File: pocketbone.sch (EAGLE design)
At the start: 61 parts, among them J1 USD_CONNECTOR, U1 24LC_32AT-I/OT, U2 OSD3358, U3 SN74LVC1G07_DCK_5, Y1 CM200C-32.768KAZF-UT, Y2 445C33D24M00000

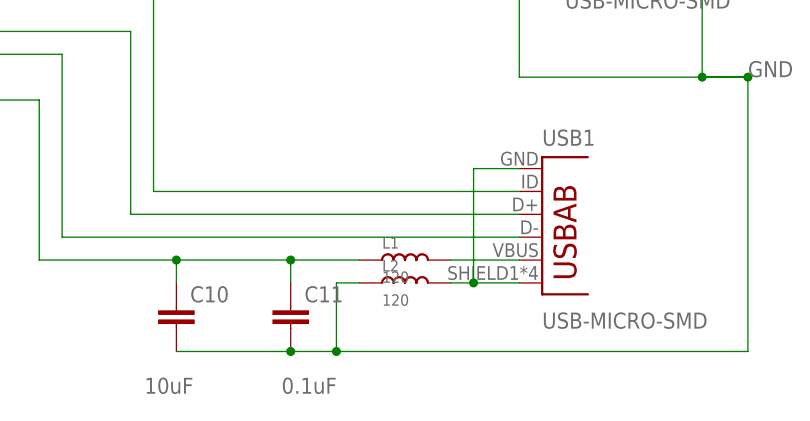
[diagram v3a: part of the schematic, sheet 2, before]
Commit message: Resize some silkscreen
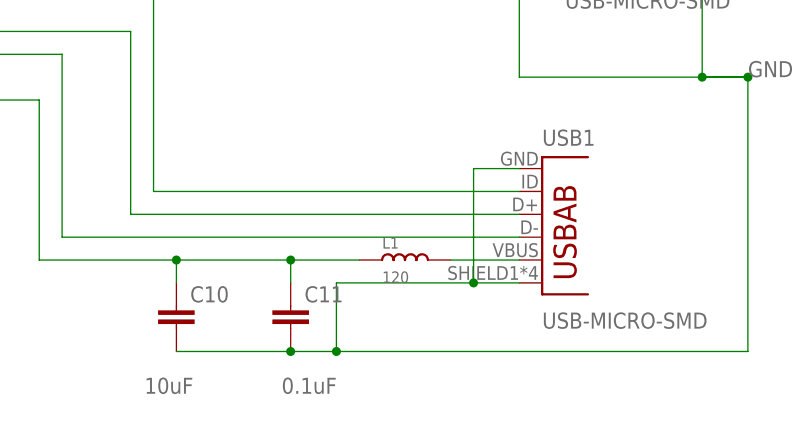
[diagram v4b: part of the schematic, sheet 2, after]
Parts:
- removed L2: 120, Seeed-OPL-Inductor:INDUCTOR/FERRITE-BEAD'0603'
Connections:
- removed net N$128: L2.2, USB1.GND, USB1.SHIELD
- net GND: now also USB1.GND, USB1.SHIELD; no longer L2.1
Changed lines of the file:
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@@
 <part name="R11" library="Strawson_Eagle_Lib" deviceset="RESISTOR" device="0402-RES" value="0"/>
 <part name="R12" library="Strawson_Eagle_Lib" deviceset="RESISTOR" device="0402-RES" value="0,DNI"/>
-<part name="L2" library="Seeed-OPL-Inductor" deviceset="INDUCTOR/FERRITE-BEAD" device="'0603'" value="120"/>
 <part name="L1" library="Seeed-OPL-Inductor" deviceset="INDUCTOR/FERRITE-BEAD" device="'0603'" value="120"/>
 <part name="C11" library="Strawson_Eagle_Lib" deviceset="CAP" device="0402-CAP" value="0.1uF"/>
@@
 <attribute name="VALUE" x="125.73" y="65.278" size="1.27" layer="96" align="center-left"/>
 </instance>
-<instance part="L2" gate="L" x="304.8" y="60.96"/>
 <instance part="L1" gate="L" x="304.8" y="63.5"/>
 <instance part="C11" gate="G$1" x="292.1" y="55.88" smashed="yes">
@@
 <wire x1="297.18" y1="53.34" x2="297.18" y2="60.96" width="0.1524" layer="91"/>
 <junction x="297.18" y="53.34"/>
-<pinref part="L2" gate="L" pin="1"/>
-<wire x1="297.18" y1="60.96" x2="299.72" y2="60.96" width="0.1524" layer="91"/>
 <pinref part="C11" gate="G$1" pin="2"/>
 <junction x="292.1" y="53.34"/>
@@
 <wire x1="320.04" y1="96.52" x2="317.5" y2="96.52" width="0.1524" layer="91"/>
 <wire x1="317.5" y1="96.52" x2="317.5" y2="83.82" width="0.1524" layer="91"/>
+<pinref part="USB1" gate="G$1" pin="SHIELD"/>
+<pinref part="USB1" gate="G$1" pin="GND"/>
+<wire x1="312.42" y1="60.96" x2="317.5" y2="60.96" width="0.1524" layer="91"/>
+<wire x1="317.5" y1="73.66" x2="312.42" y2="73.66" width="0.1524" layer="91"/>
+<wire x1="312.42" y1="73.66" x2="312.42" y2="60.96" width="0.1524" layer="91"/>
+<junction x="312.42" y="60.96"/>
+<wire x1="297.18" y1="60.96" x2="312.42" y2="60.96" width="0.1524" layer="91"/>
 </segment>
 </net>
@@
 </segment>
 </net>
-<net name="N$128" class="3">
-<segment>
-<pinref part="L2" gate="L" pin="2"/>
-<pinref part="USB1" gate="G$1" pin="SHIELD"/>
-<wire x1="309.88" y1="60.96" x2="312.42" y2="60.96" width="0.1524" layer="91"/>
-<pinref part="USB1" gate="G$1" pin="GND"/>
-<wire x1="312.42" y1="60.96" x2="317.5" y2="60.96" width="0.1524" layer="91"/>
-<wire x1="317.5" y1="73.66" x2="312.42" y2="73.66" width="0.1524" layer="91"/>
-<wire x1="312.42" y1="73.66" x2="312.42" y2="60.96" width="0.1524" layer="91"/>
-<junction x="312.42" y="60.96"/>
-</segment>
-</net>

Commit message: Reposition components
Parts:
- TP1, TP2, TP3, TP4: value TPSQB1,27 -> TPSQPAD1-17; device testpad:TPSQB1,27 -> pocketbone:TPSQPAD1-17
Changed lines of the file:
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@@
 <parts>
 <part name="U2" library="pocketbone" deviceset="OSD3358" device=""/>
-<part name="TP1" library="testpad" deviceset="TPSQ" device="B1,27">
+<part name="TP1" library="pocketbone" deviceset="TPSQ" device="PAD1-17">
 <attribute name="TP_SIGNAL_NAME" value="SYS_5V"/>
 </part>
@@
 <part name="U1" library="pocketbone" deviceset="24LC_" device="" technology="32AT-I/OT"/>
 <part name="R7" library="Strawson_Eagle_Lib" deviceset="RESISTOR" device="0402-RES" value="1.5K,1%"/>
-<part name="TP4" library="testpad" deviceset="TPSQ" device="B1,27">
+<part name="TP4" library="pocketbone" deviceset="TPSQ" device="PAD1-17">
 <attribute name="TP_SIGNAL_NAME" value="WP"/>
 </part>
@@
 <part name="J1" library="pocketbone" deviceset="USD_CONNECTOR" device=""/>
 <part name="USB1" library="pocketbone" deviceset="USB-AB" device="" value="USB-MICRO-SMD"/>
-<part name="TP2" library="testpad" deviceset="TPSQ" device="B1,27">
+<part name="TP2" library="pocketbone" deviceset="TPSQ" device="PAD1-17">
 <attribute name="TP_SIGNAL_NAME" value="5.0V"/>
 </part>
@@
 <part name="R28" library="Strawson_Eagle_Lib" deviceset="RESISTOR" device="0402-RES" value="100K,1%"/>
 <part name="R23" library="Strawson_Eagle_Lib" deviceset="RESISTOR" device="0402-RES" value="100K,1%"/>
-<part name="TP3" library="testpad" deviceset="TPSQ" device="B1,27">
+<part name="TP3" library="pocketbone" deviceset="TPSQ" device="PAD1-17">
 <attribute name="TP_SIGNAL_NAME" value="GND"/>
 </part>
